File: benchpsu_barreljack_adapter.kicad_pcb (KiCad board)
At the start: 2 copper layers, 66 x 66 mm, 22 parts, among them J1 +, J2 -, J3 DC-044K-D020, SW1 SK22D15L5, U1 HT7525-1, U2 HT7525-1 (SOT89)

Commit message: Updated project
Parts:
- R1, R2, R3, R4: value 100 -> 75
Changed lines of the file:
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@@
     (tags "resistor handsolder")
     (property "Package" "1206")
-    (property "Part Number" "")
+    (property "Part Number" "FRC1206F75R0TS")
     (property "Sheetfile" "benchpsu_barreljack_adapter.kicad_sch")
     (property "Sheetname" "")
@@
         (effects (font (size 1 1) (thickness 0.15)))
     )
-    (fp_text value "100" (at 0 1.82 90) (layer "F.Fab")
+    (fp_text value "75" (at 0 1.82 90) (layer "F.Fab")
         (effects (font (size 1 1) (thickness 0.15)))
     )
@@
     (at 161.925 128.016 180)
     (property "Package" "")
-    (property "Part Number" " 24.302.2")
+    (property "Part Number" "24.302.2")
     (property "Sheetfile" "benchpsu_barreljack_adapter.kicad_sch")
     (property "Sheetname" "")
@@
     (tags "to-92 sc-43 sc-43a sot54 PA33 transistor")
     (property "Package" "TO-92")
-    (property "Part Number" " HT7525-1")
+    (property "Part Number" "HT7525-1")
     (property "Sheetfile" "benchpsu_barreljack_adapter.kicad_sch")
     (property "Sheetname" "")
@@
     (at 142.875 128.016 180)
     (property "Package" "")
-    (property "Part Number" " 24.302.1")
+    (property "Part Number" "24.302.1")
     (property "Sheetfile" "benchpsu_barreljack_adapter.kicad_sch")
     (property "Sheetname" "")
@@
     (tags "CP Radial series Radial pin pitch 1.50mm  diameter 4mm Electrolytic Capacitor")
     (property "Package" "D4.0mm P1.50mm")
-    (property "Part Number" "")
+    (property "Part Number" "SM1061EMB072RB")
     (property "Sheetfile" "benchpsu_barreljack_adapter.kicad_sch")
     (property "Sheetname" "")
@@
     (tags "resistor handsolder")
     (property "Package" "1206")
-    (property "Part Number" "")
+    (property "Part Number" "FRC1206F75R0TS")
     (property "Sheetfile" "benchpsu_barreljack_adapter.kicad_sch")
     (property "Sheetname" "")
@@
         (effects (font (size 1 1) (thickness 0.15)))
     )
-    (fp_text value "100" (at 0 1.82 90) (layer "F.Fab")
+    (fp_text value "75" (at 0 1.82 90) (layer "F.Fab")
         (effects (font (size 1 1) (thickness 0.15)))
     )
@@
     (tags "to-92 sc-43 sc-43a sot54 PA33 transistor")
     (property "Package" "TO-92")
-    (property "Part Number" " HT7525-1")
+    (property "Part Number" "HT7525-1")
     (property "Sheetfile" "benchpsu_barreljack_adapter.kicad_sch")
     (property "Sheetname" "")
@@
     (tags "resistor handsolder")
     (property "Package" "1206")
-    (property "Part Number" "")
+    (property "Part Number" "FRC1206F75R0TS")
     (property "Sheetfile" "benchpsu_barreljack_adapter.kicad_sch")
     (property "Sheetname" "")
@@
         (effects (font (size 1 1) (thickness 0.15)))
     )
-    (fp_text value "100" (at 0 1.82 90) (layer "F.Fab")
+    (fp_text value "75" (at 0 1.82 90) (layer "F.Fab")
         (effects (font (size 1 1) (thickness 0.15)))
     )
@@
   (footprint "benchpsu_barreljack_adapter:SK22D15L5" (layer "F.Cu")
     (at 166.37 77.43 180)
+    (property "Package" "")
+    (property "Part Number" "SK22D15L5")
     (property "Sheetfile" "benchpsu_barreljack_adapter.kicad_sch")
     (property "Sheetname" "")
@@
     (tags "CP Radial series Radial pin pitch 1.50mm  diameter 4mm Electrolytic Capacitor")
     (property "Package" "D4.0mm P1.50mm")
-    (property "Part Number" "")
+    (property "Part Number" "SM1061EMB072RB")
     (property "Sheetfile" "benchpsu_barreljack_adapter.kicad_sch")
     (property "Sheetname" "")
@@
     (tags "CP Radial series Radial pin pitch 1.50mm  diameter 4mm Electrolytic Capacitor")
     (property "Package" "D4.0mm P1.50mm")
-    (property "Part Number" "")
+    (property "Part Number" "SM1061EMB072RB")
     (property "Sheetfile" "benchpsu_barreljack_adapter.kicad_sch")
     (property "Sheetname" "")
@@
     (tags "resistor handsolder")
     (property "Package" "1206")
-    (property "Part Number" "")
+    (property "Part Number" "FRC1206F75R0TS")
     (property "Sheetfile" "benchpsu_barreljack_adapter.kicad_sch")
     (property "Sheetname" "")
@@
         (effects (font (size 1 1) (thickness 0.15)))
     )
-    (fp_text value "100" (at 0 1.82 90) (layer "F.Fab")
+    (fp_text value "75" (at 0 1.82 90) (layer "F.Fab")
         (effects (font (size 1 1) (thickness 0.15)))
     )
@@
     (at 152.4 74.35)
     (property "Package" "1206")
-    (property "Part Number" " DC-044K-D020")
+    (property "Part Number" "DC-044K-D020")
     (property "Sheetfile" "benchpsu_barreljack_adapter.kicad_sch")
     (property "Sheetname" "")
@@
     (tags "CP Radial series Radial pin pitch 1.50mm  diameter 4mm Electrolytic Capacitor")
     (property "Package" "D4.0mm P1.50mm")
-    (property "Part Number" "")
+    (property "Part Number" "SM1061EMB072RB")
     (property "Sheetfile" "benchpsu_barreljack_adapter.kicad_sch")
     (property "Sheetname" "")
@@
     (pts (xy 125.4 74.6) (xy 179.4 74.6))
     (height -13.894)
-    (gr_text "54,0000 mm" (at 152.4 58.906) (layer "Dwgs.User")
+    (gr_text "54,00 mm" (at 152.4 58.906) (layer "Dwgs.User")
       (effects (font (size 1.5 1.5) (thickness 0.3)))
     )
-    (format (prefix "") (suffix "") (units 3) (units_format 1) (precision 4))
+    (format (prefix "") (suffix "") (units 3) (units_format 1) (precision 2))
     (style (thickness 0.2) (arrow_length 1.27) (text_position_mode 0) (extension_height 0.58642) (extension_offset 0.5) keep_text_aligned)
   )
@@
     (pts (xy 128.4 134.6) (xy 128.4 68.6))
     (height -29.848)
-    (gr_text "66,0000 mm" (at 96.752 101.6 90) (layer "Dwgs.User")
+    (gr_text "66,00 mm" (at 96.752 101.6 90) (layer "Dwgs.User")
       (effects (font (size 1.5 1.5) (thickness 0.3)))
     )
-    (format (prefix "") (suffix "") (units 3) (units_format 1) (precision 4))
+    (format (prefix "") (suffix "") (units 3) (units_format 1) (precision 2))
     (style (thickness 0.2) (arrow_length 1.27) (text_position_mode 0) (extension_height 0.58642) (extension_offset 0.5) keep_text_aligned)
   )
@@
     (pts (xy 179.4 128.6) (xy 179.4 74.6))
     (height 14.91)
-    (gr_text "54,0000 mm" (at 192.51 101.6 90) (layer "Dwgs.User")
+    (gr_text "54,00 mm" (at 192.51 101.6 90) (layer "Dwgs.User")
       (effects (font (size 1.5 1.5) (thickness 0.3)))
     )
-    (format (prefix "") (suffix "") (units 3) (units_format 1) (precision 4))
+    (format (prefix "") (suffix "") (units 3) (units_format 1) (precision 2))
     (style (thickness 0.2) (arrow_length 1.27) (text_position_mode 0) (extension_height 0.58642) (extension_offset 0.5) keep_text_aligned)
   )
@@
     (pts (xy 185.4 125.6) (xy 119.4 125.6))
     (height -27.308)
-    (gr_text "66,0000 mm" (at 152.4 151.108) (layer "Dwgs.User")
+    (gr_text "66,00 mm" (at 152.4 151.108) (layer "Dwgs.User")
       (effects (font (size 1.5 1.5) (thickness 0.3)))
     )
-    (format (prefix "") (suffix "") (units 3) (units_format 1) (precision 4))
+    (format (prefix "") (suffix "") (units 3) (units_format 1) (precision 2))
     (style (thickness 0.2) (arrow_length 1.27) (text_position_mode 0) (extension_height 0.58642) (extension_offset 0.5) keep_text_aligned)
   )
@@
     (pts (xy 179.4 74.6) (xy 180.848 73.406))
     (leader_length 3.81)
-    (gr_text "R 1,6 mm" (at 196.48753 70.982106) (layer "Dwgs.User")
+    (gr_text "R 1,60 mm" (at 196.48753 70.982106) (layer "Dwgs.User")
       (effects (font (size 1.5 1.5) (thickness 0.3) bold))
     )
-    (format (prefix "R ") (suffix "") (units 3) (units_format 1) (precision 4) (override_value "1,6"))
+    (format (prefix "R ") (suffix "") (units 3) (units_format 1) (precision 2) (override_value "1,60"))
+    (style (thickness 0.2) (arrow_length 1.27) (text_position_mode 0) (extension_offset 0.5) keep_text_aligned)
+  )
+  (dimension (type radial) (layer "Dwgs.User")
+    (pts (xy 176.4 77.6) (xy 182.763961 71.236039))
+    (leader_length 3.81)
+    (gr_text "R 9,00 mm" (at 198.158038 68.541962) (layer "Dwgs.User")
+      (effects (font (size 1.5 1.5) (thickness 0.3)))
+    )
+    (format (prefix "R ") (suffix "") (units 3) (units_format 1) (precision 2))
     (style (thickness 0.2) (arrow_length 1.27) (text_position_mode 0) (extension_offset 0.5) keep_text_aligned)
   )
@@
     (height 9.093)
     (orientation 0)
-    (gr_text "6,0000 mm" (at 122.4 81.893) (layer "Dwgs.User")
+    (gr_text "6,00 mm" (at 122.4 81.893) (layer "Dwgs.User")
       (effects (font (size 1.5 1.5) (thickness 0.3)))
     )
-    (format (prefix "") (suffix "") (units 3) (units_format 1) (precision 4))
+    (format (prefix "") (suffix "") (units 3) (units_format 1) (precision 2))
     (style (thickness 0.2) (arrow_length 1.27) (text_position_mode 0) (extension_height 0.58642) (extension_offset 0.5) keep_text_aligned)
   )
@@
     (height 7.95)
     (orientation 1)
-    (gr_text "6,0000 mm" (at 131.55 71.6 90) (layer "Dwgs.User")
+    (gr_text "6,00 mm" (at 131.55 71.6 90) (layer "Dwgs.User")
       (effects (font (size 1.5 1.5) (thickness 0.3)))
     )
-    (format (prefix "") (suffix "") (units 3) (units_format 1) (precision 4))
+    (format (prefix "") (suffix "") (units 3) (units_format 1) (precision 2))
     (style (thickness 0.2) (arrow_length 1.27) (text_position_mode 0) (extension_height 0.58642) (extension_offset 0.5) keep_text_aligned)
   )

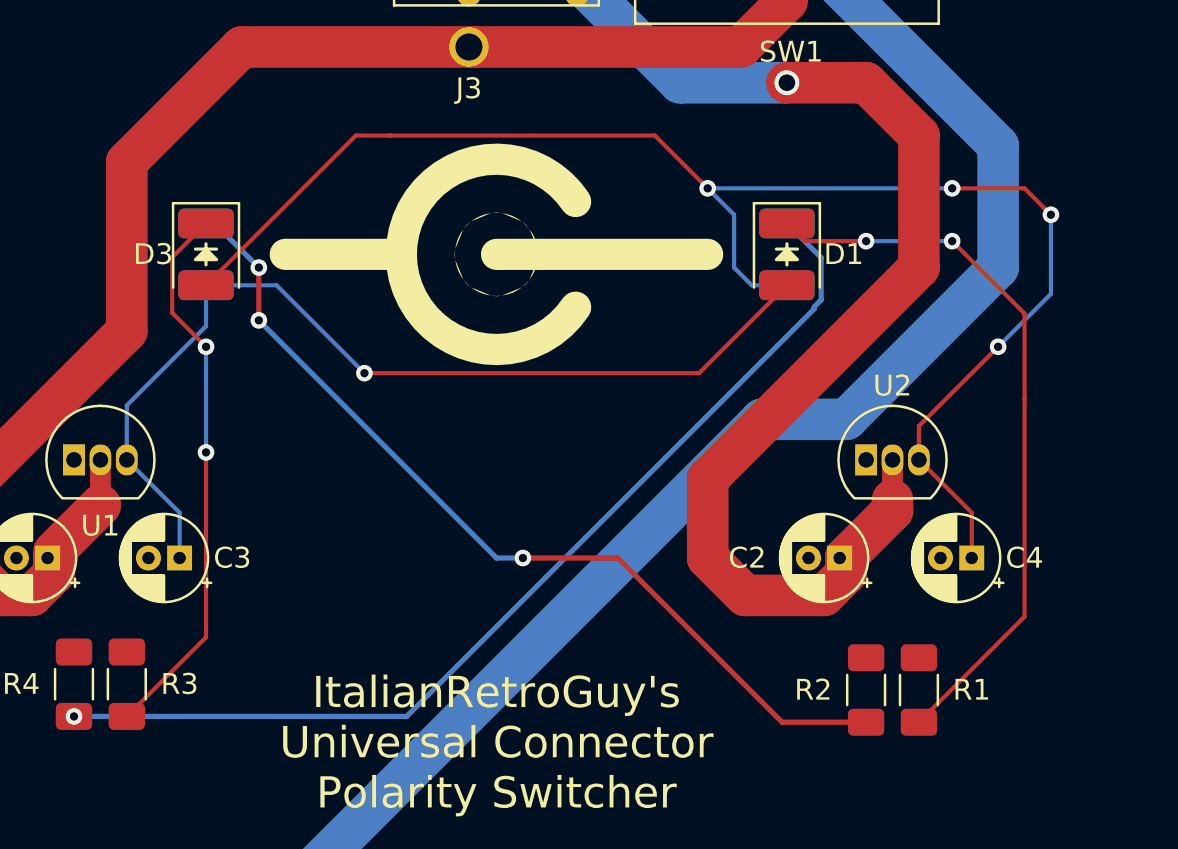
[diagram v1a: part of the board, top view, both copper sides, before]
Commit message: Updated project for better capacitor routing
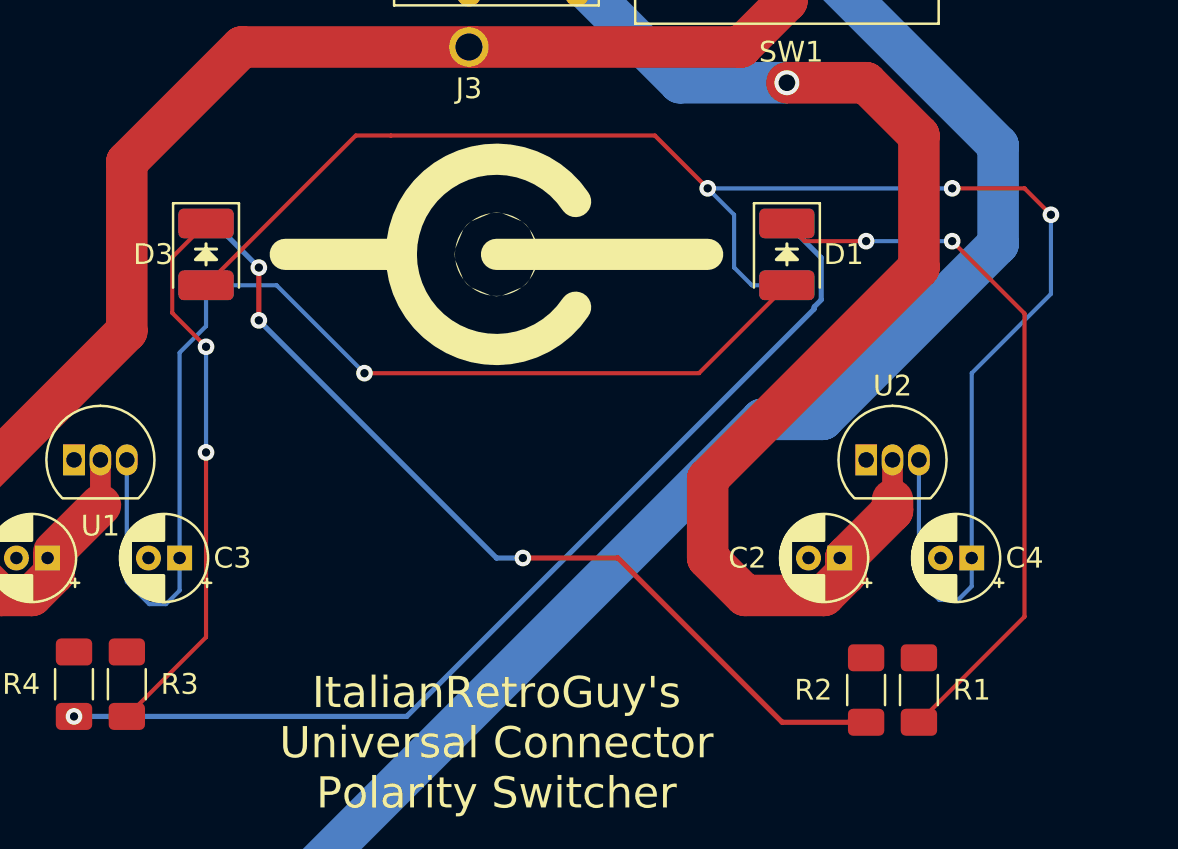
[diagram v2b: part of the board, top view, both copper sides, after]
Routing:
- net Net-(D1-A): track 47.2 -> 55.8 mm
- net Net-(D3-A): track 72.6 -> 80.9 mm, vias 4 -> 3
- net VCC: track 82.6 -> 82.0 mm
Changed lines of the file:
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@@
     (property "ki_description" "Generic screw terminal, single row, 01x01, script generated (kicad-library-utils/schlib/autogen/connector/)")
     (property "ki_keywords" "screw terminal")
-    (attr through_hole)
+    (attr smd)
     (fp_text reference "J2" (at 6.477 0.254) (layer "F.SilkS")
         (effects (font (size 1 1) (thickness 0.15)))
@@
     (property "ki_description" "Generic screw terminal, single row, 01x01, script generated (kicad-library-utils/schlib/autogen/connector/)")
     (property "ki_keywords" "screw terminal")
-    (attr through_hole)
+    (attr smd)
     (fp_text reference "J1" (at 6.477 0.254) (layer "F.SilkS")
         (effects (font (size 1 1) (thickness 0.15)))
@@
   (segment (start 146.05 97.79) (end 162.1425 97.79) (width 0.2) (layer "F.Cu") (net 4))
   (via (at 146.05 97.79) (size 0.8) (drill 0.4) (layers "F.Cu" "B.Cu") (net 4))
-  (segment (start 137.16 104.5) (end 134.62 101.96) (width 0.2) (layer "B.Cu") (net 4))
+  (segment (start 134.62 107.82) (end 135.7 108.9) (width 0.2) (layer "B.Cu") (net 4))
+  (segment (start 135.7 108.9) (end 136.5 108.9) (width 0.2) (layer "B.Cu") (net 4))
+  (segment (start 137.16 106.68) (end 137.16 96.80005) (width 0.2) (layer "B.Cu") (net 4))
   (segment (start 138.43 95.53005) (end 138.43 93.5625) (width 0.2) (layer "B.Cu") (net 4))
   (segment (start 138.43 93.5625) (end 141.8225 93.5625) (width 0.2) (layer "B.Cu") (net 4))
   (segment (start 141.8225 93.5625) (end 146.05 97.79) (width 0.2) (layer "B.Cu") (net 4))
-  (segment (start 137.16 106.68) (end 137.16 104.5) (width 0.2) (layer "B.Cu") (net 4))
-  (segment (start 134.62 99.34005) (end 138.43 95.53005) (width 0.2) (layer "B.Cu") (net 4))
-  (segment (start 134.62 101.96) (end 134.62 99.34005) (width 0.2) (layer "B.Cu") (net 4))
-  (segment (start 175.26 106.68) (end 175.26 104.5) (width 0.2) (layer "F.Cu") (net 5))
+  (segment (start 134.62 101.96) (end 134.62 107.82) (width 0.2) (layer "B.Cu") (net 4))
+  (segment (start 137.16 96.80005) (end 138.43 95.53005) (width 0.2) (layer "B.Cu") (net 4))
+  (segment (start 137.16 108.24) (end 137.16 106.68) (width 0.2) (layer "B.Cu") (net 4))
+  (segment (start 136.5 108.9) (end 137.16 108.24) (width 0.2) (layer "B.Cu") (net 4))
   (segment (start 160.02 86.36) (end 162.56 88.9) (width 0.2) (layer "F.Cu") (net 5))
   (segment (start 177.8 88.9) (end 174.3195 88.9) (width 0.2) (layer "F.Cu") (net 5))
-  (segment (start 172.72 101.96) (end 172.72 100.33) (width 0.2) (layer "F.Cu") (net 5))
   (segment (start 138.43 93.5625) (end 145.6325 86.36) (width 0.2) (layer "F.Cu") (net 5))
   (segment (start 147.32 86.36) (end 160.02 86.36) (width 0.2) (layer "F.Cu") (net 5))
   (segment (start 145.6325 86.36) (end 147.32 86.36) (width 0.2) (layer "F.Cu") (net 5))
-  (segment (start 175.26 104.5) (end 172.72 101.96) (width 0.2) (layer "F.Cu") (net 5))
   (segment (start 179.07 90.17) (end 177.8 88.9) (width 0.2) (layer "F.Cu") (net 5))
-  (segment (start 172.72 100.33) (end 176.53 96.52) (width 0.2) (layer "F.Cu") (net 5))
   (via (at 179.07 90.17) (size 0.8) (drill 0.4) (layers "F.Cu" "B.Cu") (net 5))
-  (via (at 176.53 96.52) (size 0.8) (drill 0.4) (layers "F.Cu" "B.Cu") (net 5))
   (via (at 162.56 88.9) (size 0.8) (drill 0.4) (layers "F.Cu" "B.Cu") (net 5))
   (via (at 174.3195 88.9) (size 0.8) (drill 0.4) (layers "F.Cu" "B.Cu") (net 5))
   (segment (start 163.83 90.17) (end 163.83 92.71) (width 0.2) (layer "B.Cu") (net 5))
   (segment (start 174.3195 88.9) (end 162.56 88.9) (width 0.2) (layer "B.Cu") (net 5))
-  (segment (start 176.53 96.52) (end 179.07 93.98) (width 0.2) (layer "B.Cu") (net 5))
+  (segment (start 172.72 107.72) (end 173.7 108.7) (width 0.2) (layer "B.Cu") (net 5))
+  (segment (start 175.26 97.79) (end 179.07 93.98) (width 0.2) (layer "B.Cu") (net 5))
+  (segment (start 175.26 108.04) (end 175.26 106.68) (width 0.2) (layer "B.Cu") (net 5))
+  (segment (start 173.7 108.7) (end 174.6 108.7) (width 0.2) (layer "B.Cu") (net 5))
   (segment (start 162.56 88.9) (end 163.83 90.17) (width 0.2) (layer "B.Cu") (net 5))
   (segment (start 163.83 92.71) (end 164.6825 93.5625) (width 0.2) (layer "B.Cu") (net 5))
+  (segment (start 174.6 108.7) (end 175.26 108.04) (width 0.2) (layer "B.Cu") (net 5))
   (segment (start 179.07 93.98) (end 179.07 90.17) (width 0.2) (layer "B.Cu") (net 5))
   (segment (start 164.6825 93.5625) (end 166.37 93.5625) (width 0.2) (layer "B.Cu") (net 5))
+  (segment (start 175.26 106.68) (end 175.26 97.79) (width 0.2) (layer "B.Cu") (net 5))
+  (segment (start 172.72 101.96) (end 172.72 107.72) (width 0.2) (layer "B.Cu") (net 5))
   (segment (start 170.18 91.44) (end 167.2225 91.44) (width 0.2) (layer "F.Cu") (net 6))
-  (segment (start 177.8 99.06) (end 177.8 94.9205) (width 0.2) (layer "F.Cu") (net 6))
-  (segment (start 172.72 114.58) (end 177.8 109.5) (width 0.2) (layer "F.Cu") (net 6))
+  (segment (start 174.3195 91.44) (end 177.8 94.9205) (width 0.2) (layer "F.Cu") (net 6))
   (segment (start 167.2225 91.44) (end 166.37 90.5875) (width 0.2) (layer "F.Cu") (net 6))
-  (segment (start 177.8 109.5) (end 177.8 99.06) (width 0.2) (layer "F.Cu") (net 6))
-  (segment (start 177.8 94.9205) (end 174.3195 91.44) (width 0.2) (layer "F.Cu") (net 6))
+  (segment (start 177.8 94.9205) (end 177.8 109.5) (width 0.2) (layer "F.Cu") (net 6))
+  (segment (start 177.8 109.5) (end 172.72 114.58) (width 0.2) (layer "F.Cu") (net 6))
   (via (at 170.18 91.44) (size 0.8) (drill 0.4) (layers "F.Cu" "B.Cu") (net 6))
   (via (at 174.3195 91.44) (size 0.8) (drill 0.4) (layers "F.Cu" "B.Cu") (net 6))
@@
   (segment (start 167.683172 94.6) (end 167.683172 94.698828) (width 0.25) (layer "B.Cu") (net 9))
   (segment (start 166.37 90.5875) (end 168.02 92.2375) (width 0.25) (layer "B.Cu") (net 9))
+  (segment (start 176.53 86.84) (end 176.53 91.57) (width 2) (layer "B.Cu") (net 10))
   (segment (start 170.18 76.87) (end 168.37 78.68) (width 2) (layer "B.Cu") (net 10))
+  (segment (start 142.875 122.301) (end 142.875 129.306) (width 2) (layer "B.Cu") (net 10))
+  (segment (start 168.09 100.01) (end 165.166 100.01) (width 2) (layer "B.Cu") (net 10))
+  (segment (start 176.53 91.57) (end 168.09 100.01) (width 2) (layer "B.Cu") (net 10))
   (segment (start 164.37 75.472894) (end 166.182894 73.66) (width 2) (layer "B.Cu") (net 10))
+  (segment (start 165.166 100.01) (end 142.875 122.301) (width 2) (layer "B.Cu") (net 10))
   (segment (start 166.182894 73.66) (end 168.91 73.66) (width 2) (layer "B.Cu") (net 10))
   (segment (start 170.18 74.93) (end 170.18 76.87) (width 2) (layer "B.Cu") (net 10))
   (segment (start 164.37 76.18) (end 164.37 75.472894) (width 2) (layer "B.Cu") (net 10))
-  (segment (start 142.875 122.301) (end 142.875 129.306) (width 2) (layer "B.Cu") (net 10))
-  (segment (start 165.166 100.01) (end 142.875 122.301) (width 2) (layer "B.Cu") (net 10))
+  (segment (start 168.91 73.66) (end 170.18 74.93) (width 2) (layer "B.Cu") (net 10))
   (segment (start 168.37 78.68) (end 176.53 86.84) (width 2) (layer "B.Cu") (net 10))
-  (segment (start 168.91 73.66) (end 170.18 74.93) (width 2) (layer "B.Cu") (net 10))
-  (segment (start 176.53 86.84) (end 176.53 92.71) (width 2) (layer "B.Cu") (net 10))
-  (segment (start 176.53 92.71) (end 169.23 100.01) (width 2) (layer "B.Cu") (net 10))
-  (segment (start 169.23 100.01) (end 165.166 100.01) (width 2) (layer "B.Cu") (net 10))
   (zone (net 2) (net_name "GND") (layers "F&B.Cu") (hatch edge 0.508)
     (connect_pads yes (clearance 0.508))
